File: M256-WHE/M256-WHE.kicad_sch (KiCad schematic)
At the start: 253 parts, among them J1 JST_SH, J2 TC2030, SW1 TS-1187A-B-A-B, SW2 TS-1187A-B-A-B, U1 USBLC6-2SC6, U2 TLV75733PDBV, U3 XC6206P332MR-G, U4 STM32F446RET6, Y1 X322516MLB4SI

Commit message: :sparkles: change OH49E-S Hall sensors to DRV5055A3
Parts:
- HE1, HE10, HE11, HE12, HE13, HE14, HE15, HE16, HE17, HE18, HE19, HE2, HE20, HE21, HE22, HE23, HE24, HE25, HE26, HE27, HE28, HE29, HE3, HE30, HE31, HE32, HE33, HE34, HE35, HE36, HE37, HE38, HE39, HE4, HE40, HE41, HE42, HE43, HE44, HE45, HE46, HE47, HE48, HE49, HE5, HE50, HE51, HE52, HE53, HE54, HE55, HE56, HE57, HE58, HE59, HE6, HE60, HE61, HE62, HE63, HE64, HE65, HE66, HE67, HE68, HE7, HE8, HE9: value OH49E-S -> DRV5055A3QDBZR; symbol M256-WHE:OH49E-S -> M256-WHE:DRV5055A3xDBZx

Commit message: :sparkles: new board with at32f405
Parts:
- removed HE1, HE10, HE11, HE12, HE13, HE14, HE15, HE16, HE17, HE18, HE19, HE2, HE20, HE21, HE22, HE23, HE24, HE25, HE26, HE27, HE28, HE29, HE3, HE30, HE31, HE32, HE33, HE34, HE35, HE36, HE37, HE38, HE39, HE4, HE40, HE41, HE42, HE43, HE44, HE45, HE46, HE47, HE48, HE49, HE5, HE50, HE51, HE52, HE53, HE54, HE55, HE56, HE57, HE58, HE59, HE6, HE60, HE61, HE62, HE63, HE64, HE65, HE66, HE67, HE68, HE7, HE8, HE9: DRV5055A3QDBZR, Package_TO_SOT_SMD:SOT-23-3, symbol M256-WHE:DRV5055A3xDBZx
- removed J2: TC2030, Connector:Tag-Connect_TC2030-IDC-FP_2x03_P1.27mm_Vertical, symbol Connector:Conn_ARM_SWD_TagConnect_TC2030
- removed U4: STM32F446RET6, Package_QFP:LQFP-64_10x10mm_P0.5mm, symbol MCU_ST_STM32F4:STM32F446RETx
- added C100, C102, C104, C106, C108, C110, C112, C114, C116, C118, C120, C122, C124, C126, C128, C130, C132, C134, C136, C94, C96, C98: 4.7n, Capacitor_SMD:C_0402_1005Metric, symbol Device:C
- added C101, C103, C105, C107, C109, C111, C113, C115, C117, C119, C121, C123, C125, C127, C129, C131, C133, C135, C137, C138, C139, C140, C141, C142, C143, C144, C145, C152, C153, C154, C156, C158, C95, C97, C99: 100n, Capacitor_SMD:C_0402_1005Metric, symbol Device:C
- added C146, C147: 2.2u, Capacitor_SMD:C_0603_1608Metric, symbol Device:C
- added C148, C149, C157: 1u, Capacitor_SMD:C_0603_1608Metric, symbol Device:C
- added C150, C151: 30p, Capacitor_SMD:C_0603_1608Metric, symbol Device:C
- added C155: 10u, Capacitor_SMD:C_0603_1608Metric, symbol Device:C
- added HE1, HE10, HE11, HE12, HE13, HE14, HE15, HE16, HE17, HE18, HE19, HE2, HE20, HE21, HE22, HE23, HE24, HE25, HE26, HE27, HE28, HE29, HE3, HE30, HE31, HE32, HE33, HE34, HE35, HE36, HE37, HE38, HE39, HE4, HE40, HE41, HE42, HE43, HE44, HE45, HE46, HE47, HE48, HE49, HE5, HE50, HE51, HE52, HE53, HE54, HE55, HE56, HE57, HE58, HE59, HE6, HE60, HE61, HE62, HE63, HE64, HE65, HE66, HE67, HE68, HE7, HE8, HE9: MT9102ET, Package_TO_SOT_SMD:SOT-23-3, symbol M256-WHE:MT9102ET
- added U4: AT32F405RCT7, Package_QFP:LQFP-64_10x10mm_P0.5mm, symbol M256-WHE:AT32F405RxT7
- C10, C12, C14, C16, C18, C2, C20, C22, C24, C26, C28, C30, C32, C34, C36, C38, C4, C40, C42, C44, C46, C48, C50, C52, C54, C56, C58, C6, C60, C62, C64, C66, C68, C70, C72, C74, C76, C8, C84, C86: value 100n -> 4.7n
- C78: value 2.2u -> 4.7n; footprint Capacitor_SMD:C_0603_1608Metric -> Capacitor_SMD:C_0402_1005Metric
- C79: value 2.2u -> 100n; footprint Capacitor_SMD:C_0603_1608Metric -> Capacitor_SMD:C_0402_1005Metric
- C80, C90: value 1u -> 4.7n; footprint Capacitor_SMD:C_0603_1608Metric -> Capacitor_SMD:C_0402_1005Metric
- C81: value 1u -> 100n; footprint Capacitor_SMD:C_0603_1608Metric -> Capacitor_SMD:C_0402_1005Metric
- C82: value 4.7u -> 4.7n; footprint Capacitor_SMD:C_0603_1608Metric -> Capacitor_SMD:C_0402_1005Metric
- C88: value 10u -> 4.7n; footprint Capacitor_SMD:C_0603_1608Metric -> Capacitor_SMD:C_0402_1005Metric
- C92: value 10p -> 4.7n
- C93: value 10p -> 100n
- R1, R2: value 10k -> 12k
- Y1: value X322516MLB4SI -> X322512MSB4SI
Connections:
- net BOOT1 is gone; now on net GND: R2.1
- net VCAP is gone; now on net HE41: C82.1
- net +3.3V: now also C149.1, C152.1, C153.1, C154.1, C155.1, U4.1 (VDD), U4.36 (VDD), U4.64 (VDD); no longer C81.1, C83.1, C84.1, C85.1, C86.1, C87.1, C88.1
- net +3.3VA: now also C81.1, C83.1, C85.1, C87.1, C91.1, C93.1, C101.1, C103.1, C105.1, C107.1, C109.1, C111.1, C113.1, C115.1, C117.1, C119.1, C121.1, C123.1, C125.1, C127.1, C129.1, C131.1, C133.1, C135.1, C137.1, C138.1, C139.1, C140.1, C141.1, C142.1, C143.1, C144.1, C145.1, C147.1, C156.1, C157.1, C95.1, C97.1, C99.1, HE1.1 (VCC), HE10.1 (VCC), HE11.1 (VCC), HE12.1 (VCC), HE13.1 (VCC), HE14.1 (VCC), HE15.1 (VCC), HE16.1 (VCC), HE17.1 (VCC), HE18.1 (VCC), HE19.1 (VCC), HE2.1 (VCC), HE20.1 (VCC), HE21.1 (VCC), HE22.1 (VCC), HE23.1 (VCC), HE24.1 (VCC), HE25.1 (VCC), HE26.1 (VCC), HE27.1 (VCC), HE28.1 (VCC), HE29.1 (VCC), HE3.1 (VCC), HE30.1 (VCC), HE31.1 (VCC), HE32.1 (VCC), HE33.1 (VCC), HE34.1 (VCC), HE35.1 (VCC), HE36.1 (VCC), HE37.1 (VCC), HE38.1 (VCC), HE39.1 (VCC), HE4.1 (VCC), HE40.1 (VCC), HE41.1 (VCC), HE42.1 (VCC), HE43.1 (VCC), HE44.1 (VCC), HE45.1 (VCC), HE46.1 (VCC), HE47.1 (VCC), HE48.1 (VCC), HE49.1 (VCC), HE5.1 (VCC), HE50.1 (VCC), HE51.1 (VCC), HE52.1 (VCC), HE53.1 (VCC), HE54.1 (VCC), HE55.1 (VCC), HE56.1 (VCC), HE57.1 (VCC), HE58.1 (VCC), HE59.1 (VCC), HE6.1 (VCC), HE60.1 (VCC), HE61.1 (VCC), HE62.1 (VCC), HE63.1 (VCC), HE64.1 (VCC), HE65.1 (VCC), HE66.1 (VCC), HE67.1 (VCC), HE68.1 (VCC), HE7.1 (VCC), HE8.1 (VCC), HE9.1 (VCC), U4.13 (VDDA); no longer C10.1, C12.1, C14.1, C16.1, C18.1, C2.1, C20.1, C22.1, C24.1, C26.1, C28.1, C30.1, C32.1, C34.1, C36.1, C38.1, C4.1, C40.1, C42.1, C44.1, C46.1, C48.1, C50.1, C52.1, C54.1, C56.1, C58.1, C6.1, C60.1, C62.1, C64.1, C66.1, C68.1, C70.1, C72.1, C74.1, C76.1, C8.1, C90.1
- net +5V: now also C146.1, C148.1; no longer C78.1, C80.1
- net BOOT0: now also U4.60 (PF11/BOOT0)
- net GND: now also C91.2, C100.2, C101.2, C102.2, C103.2, C104.2, C105.2, C106.2, C107.2, C108.2, C109.2, C110.2, C111.2, C112.2, C113.2, C114.2, C115.2, C116.2, C117.2, C118.2, C119.2, C120.2, C121.2, C122.2, C123.2, C124.2, C125.2, C126.2, C127.2, C128.2, C129.2, C130.2, C131.2, C132.2, C133.2, C134.2, C135.2, C136.2, C137.2, C138.2, C139.2, C140.2, C141.2, C142.2, C143.2, C144.2, C145.2, C146.2, C147.2, C148.2, C149.2, C150.2, C151.2, C152.2, C153.2, C154.2, C155.2, C156.2, C157.2, C158.2, C94.2, C95.2, C96.2, C97.2, C98.2, C99.2, HE1.3 (GND), HE10.3 (GND), HE11.3 (GND), HE12.3 (GND), HE13.3 (GND), HE14.3 (GND), HE15.3 (GND), HE16.3 (GND), HE17.3 (GND), HE18.3 (GND), HE19.3 (GND), HE2.3 (GND), HE20.3 (GND), HE21.3 (GND), HE22.3 (GND), HE23.3 (GND), HE24.3 (GND), HE25.3 (GND), HE26.3 (GND), HE27.3 (GND), HE28.3 (GND), HE29.3 (GND), HE3.3 (GND), HE30.3 (GND), HE31.3 (GND), HE32.3 (GND), HE33.3 (GND), HE34.3 (GND), HE35.3 (GND), HE36.3 (GND), HE37.3 (GND), HE38.3 (GND), HE39.3 (GND), HE4.3 (GND), HE40.3 (GND), HE41.3 (GND), HE42.3 (GND), HE43.3 (GND), HE44.3 (GND), HE45.3 (GND), HE46.3 (GND), HE47.3 (GND), HE48.3 (GND), HE49.3 (GND), HE5.3 (GND), HE50.3 (GND), HE51.3 (GND), HE52.3 (GND), HE53.3 (GND), HE54.3 (GND), HE55.3 (GND), HE56.3 (GND), HE57.3 (GND), HE58.3 (GND), HE59.3 (GND), HE6.3 (GND), HE60.3 (GND), HE61.3 (GND), HE62.3 (GND), HE63.3 (GND), HE64.3 (GND), HE65.3 (GND), HE66.3 (GND), HE67.3 (GND), HE68.3 (GND), HE7.3 (GND), HE8.3 (GND), HE9.3 (GND), U4.12 (VSSA), U4.31 (VSS), U4.63 (VSS); no longer C91.1, R2.2
- net HE1: now also C2.1, HE1.2 (OUT)
- net HE10: now also C20.1, HE10.2 (OUT)
- net HE11: now also C22.1, HE11.2 (OUT)
- net HE12: now also C24.1, HE12.2 (OUT)
- net HE13: now also C26.1, HE13.2 (OUT)
- net HE14: now also C28.1, HE14.2 (OUT)
- net HE15: now also C30.1, HE15.2 (OUT)
- net HE16: now also C32.1, HE16.2 (OUT)
- net HE17: now also C34.1, HE17.2 (OUT)
- net HE18: now also C36.1, HE18.2 (OUT)
- net HE19: now also C38.1, HE19.2 (OUT)
- net HE2: now also C4.1, HE2.2 (OUT)
- net HE20: now also C40.1, HE20.2 (OUT)
- net HE21: now also C42.1, HE21.2 (OUT)
- net HE22: now also C44.1, HE22.2 (OUT)
- net HE23: now also C46.1, HE23.2 (OUT)
- net HE24: now also C48.1, HE24.2 (OUT)
- net HE25: now also C50.1, HE25.2 (OUT)
- net HE26: now also C52.1, HE26.2 (OUT)
- net HE27: now also C54.1, HE27.2 (OUT)
- net HE28: now also C56.1, HE28.2 (OUT)
- net HE29: now also C58.1, HE29.2 (OUT)
- net HE3: now also C6.1, HE3.2 (OUT)
- net HE30: now also C60.1, HE30.2 (OUT)
- net HE31: now also C62.1, HE31.2 (OUT)
- net HE32: now also C64.1, HE32.2 (OUT)
- net HE33: now also C66.1, HE33.2 (OUT)
- net HE34: now also C68.1, HE34.2 (OUT)
- net HE35: now also C70.1, HE35.2 (OUT)
- net HE36: now also C72.1, HE36.2 (OUT)
- net HE37: now also C74.1, HE37.2 (OUT)
- net HE38: now also C76.1, HE38.2 (OUT)
- net HE39: now also C78.1, HE39.2 (OUT)
- net HE4: now also C8.1, HE4.2 (OUT)
- net HE40: now also C80.1, HE40.2 (OUT)
- net HE41: now also HE41.2 (OUT)
- net HE42: now also C84.1, HE42.2 (OUT)
- net HE43: now also C86.1, HE43.2 (OUT)
- net HE44: now also C88.1, HE44.2 (OUT)
- net HE45: now also C90.1, HE45.2 (OUT)
- net HE46: now also C92.1, HE46.2 (OUT)
- net HE47: now also C94.1, HE47.2 (OUT)
- net HE48: now also C96.1, HE48.2 (OUT)
- net HE49: now also C98.1, HE49.2 (OUT)
- net HE5: now also C10.1, HE5.2 (OUT)
- net HE50: now also C100.1, HE50.2 (OUT)
- net HE51: now also C102.1, HE51.2 (OUT)
- net HE52: now also C104.1, HE52.2 (OUT)
- net HE53: now also C106.1, HE53.2 (OUT)
- net HE54: now also C108.1, HE54.2 (OUT)
- net HE55: now also C110.1, HE55.2 (OUT)
- net HE56: now also C112.1, HE56.2 (OUT)
- net HE57: now also C114.1, HE57.2 (OUT)
- net HE58: now also C116.1, HE58.2 (OUT)
- net HE59: now also C118.1, HE59.2 (OUT)
- net HE6: now also C12.1, HE6.2 (OUT)
- net HE60: now also C120.1, HE60.2 (OUT)
- net HE61: now also C122.1, HE61.2 (OUT)
- net HE62: now also C124.1, HE62.2 (OUT)
- net HE63: now also C126.1, HE63.2 (OUT)
- net HE64: now also C128.1, HE64.2 (OUT)
- net HE65: now also C130.1, HE65.2 (OUT)
- net HE66: now also C132.1, HE66.2 (OUT)
- net HE67: now also C134.1, HE67.2 (OUT)
- net HE68: now also C136.1, HE68.2 (OUT)
- net HE7: now also C14.1, HE7.2 (OUT)
- net HE8: now also C16.1, HE8.2 (OUT)
- net HE9: now also C18.1, HE9.2 (OUT)
- net MUX_OUT_1: now also U4.27 (PB1)
- net MUX_OUT_2: now also U4.17 (PA3)
- net MUX_OUT_3: now also U4.26 (PB0)
- net MUX_OUT_4: now also U4.20 (PA4)
- net MUX_OUT_5: now also U4.25 (PC5)
- net MUX_OUT_6: now also U4.21 (PA5)
- net MUX_OUT_7: now also U4.24 (PC4)
- net MUX_OUT_8: now also U4.22 (PA6)
- net MUX_OUT_9: now also U4.23 (PA7)
- net MUX_SELECT_0: now also U4.32 (PB13)
- net MUX_SELECT_1: now also U4.30 (PB12)
- net MUX_SELECT_2: now also U4.29 (PB10)
- net NRST: now also C158.1, U4.7 (NRST); no longer C91.2
- net USB_D+: now also U4.35 (OTGHS1_D+)
- net USB_D-: now also U4.34 (OTGHS1_D-)
- net RCC_OSC_IN renamed HEXT_IN
- net HEXT_IN: now also C150.1, U4.5 (PF0/HEXT_IN); no longer C92.1
- net RCC_OSC_OUT renamed HEXT_OUT
- net HEXT_OUT: now also C151.1, U4.6 (PF1/HEXT_OUT); no longer C93.1
- new net: R2.2, U4.33 (OTGHS1_R)
- no-connect marks 31 -> 39
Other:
- moved on the sheet: AM1

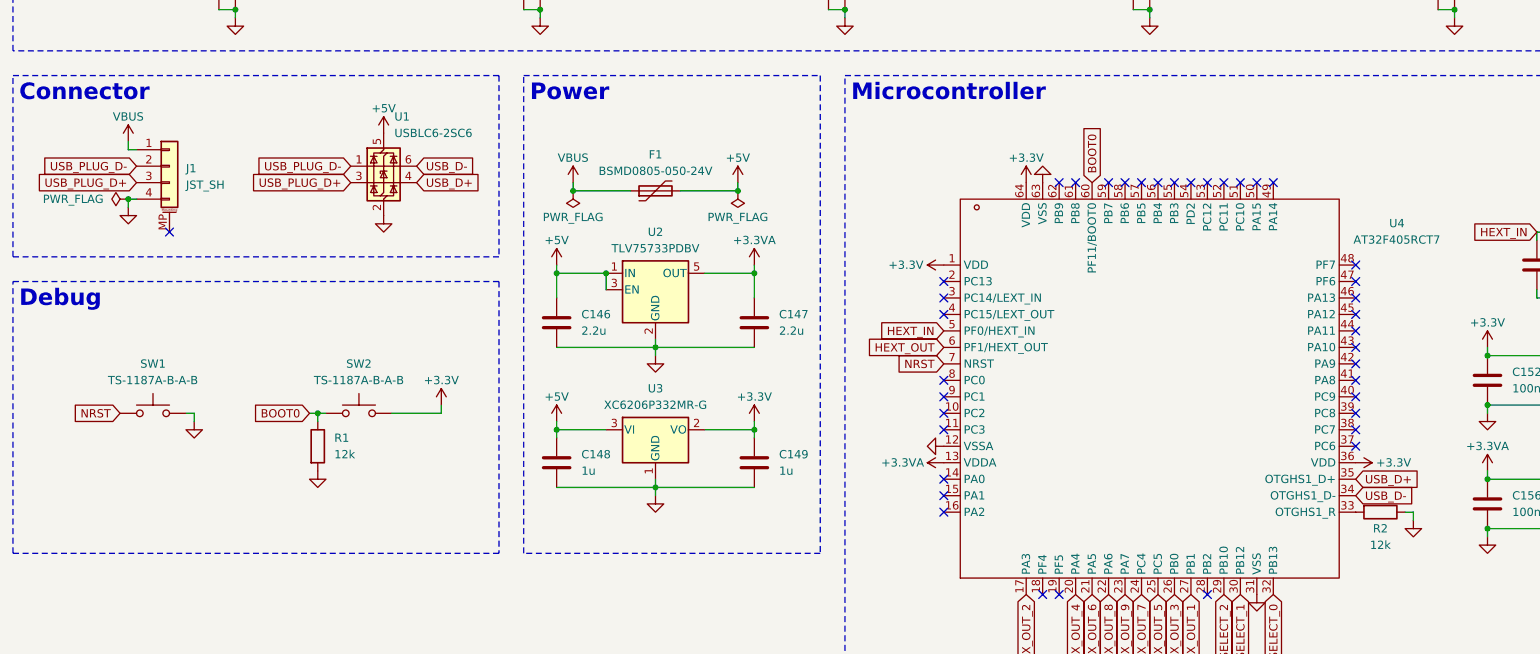
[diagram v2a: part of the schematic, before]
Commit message: :sparkles: add TC2030 connector
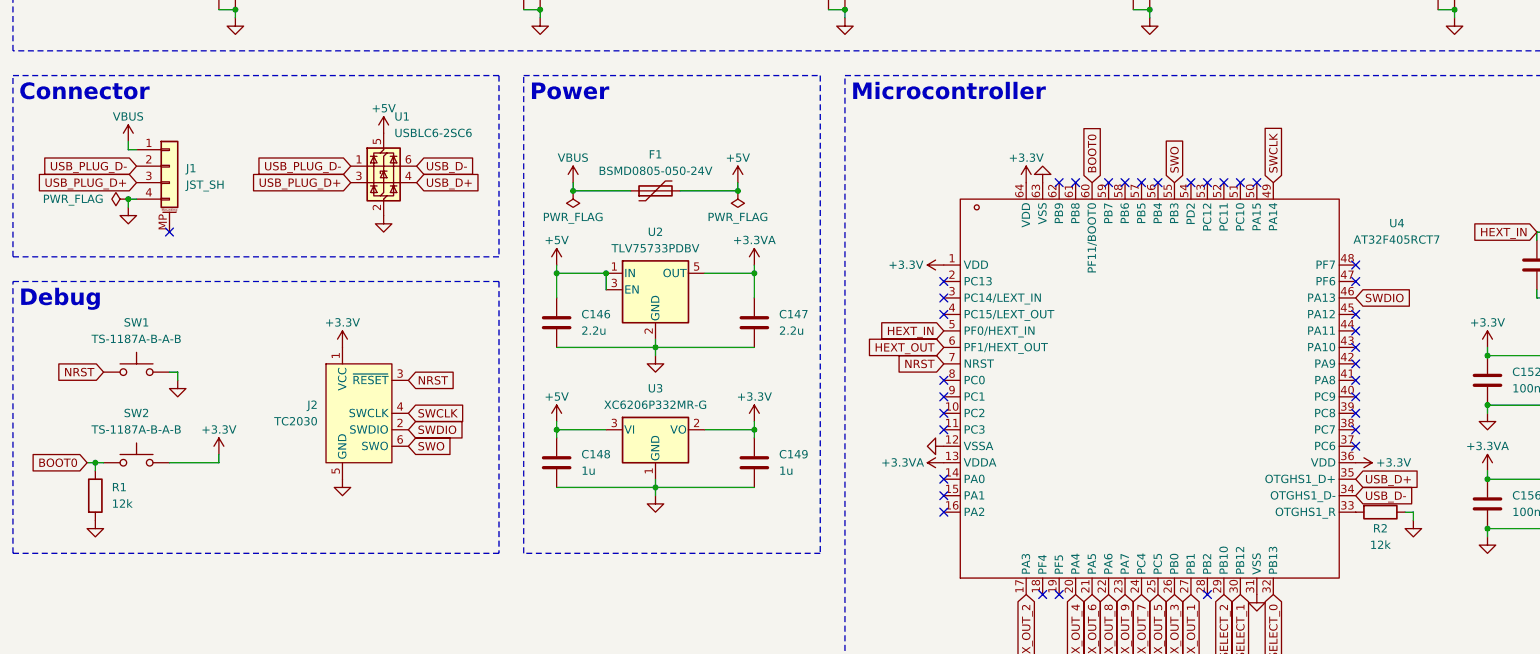
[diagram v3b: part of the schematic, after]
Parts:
- added J2: TC2030, Connector:Tag-Connect_TC2030-IDC-FP_2x03_P1.27mm_Vertical, symbol Connector:Conn_ARM_SWD_TagConnect_TC2030
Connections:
- net +3.3V: now also J2.1 (VCC)
- net GND: now also J2.5 (GND)
- net NRST: now also J2.3 (~{RESET})
- net SWDIO: now reaches U4.46 (PA13)
- net SWDIO: now also J2.2 (SWDIO)
- net SWCLK: now reaches U4.49 (PA14)
- net SWCLK: now also J2.4 (SWCLK)
- net SWO: now reaches U4.55 (PB3)
- net SWO: now also J2.6 (SWO)
- no-connect marks 39 -> 36
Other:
- moved on the sheet: R1, SW1, SW2
